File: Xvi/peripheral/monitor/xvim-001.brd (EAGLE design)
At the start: 47 x 72 mm, 7 parts

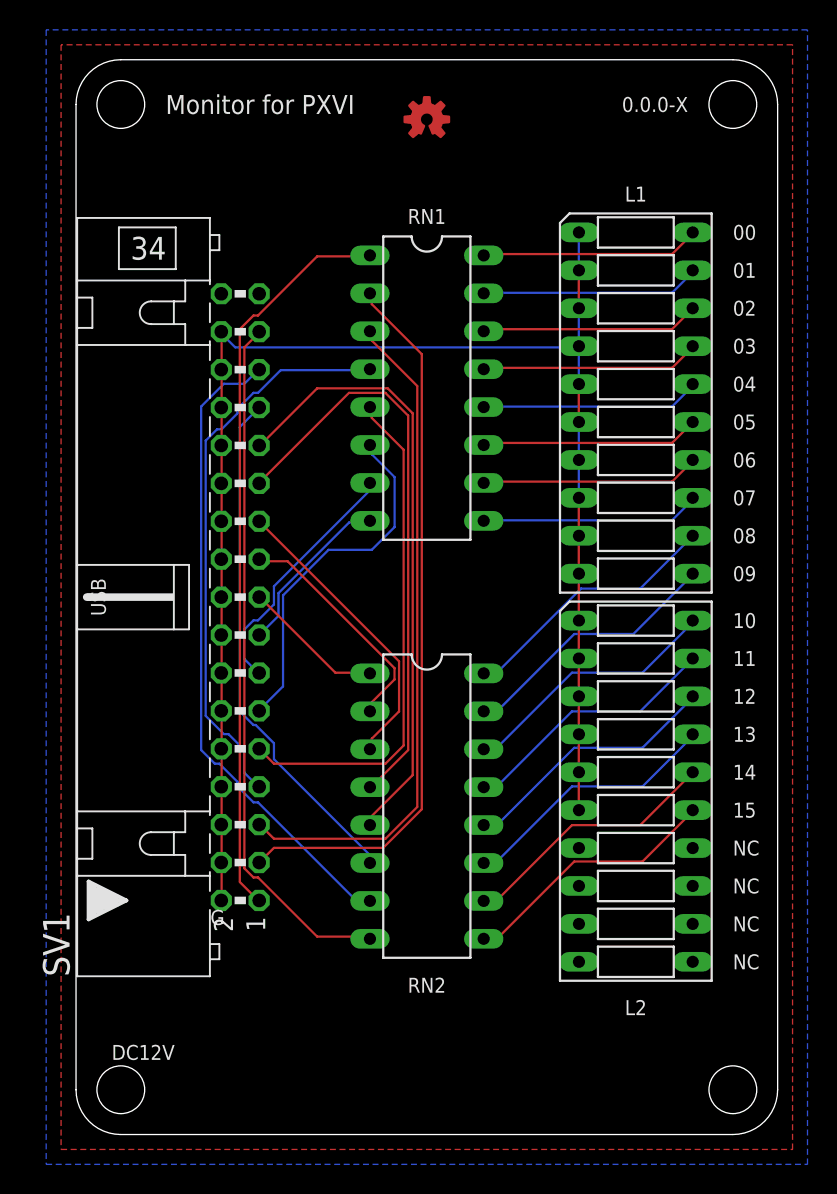
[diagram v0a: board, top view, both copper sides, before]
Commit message: Fixed positioning error of Monitor for PXVI.
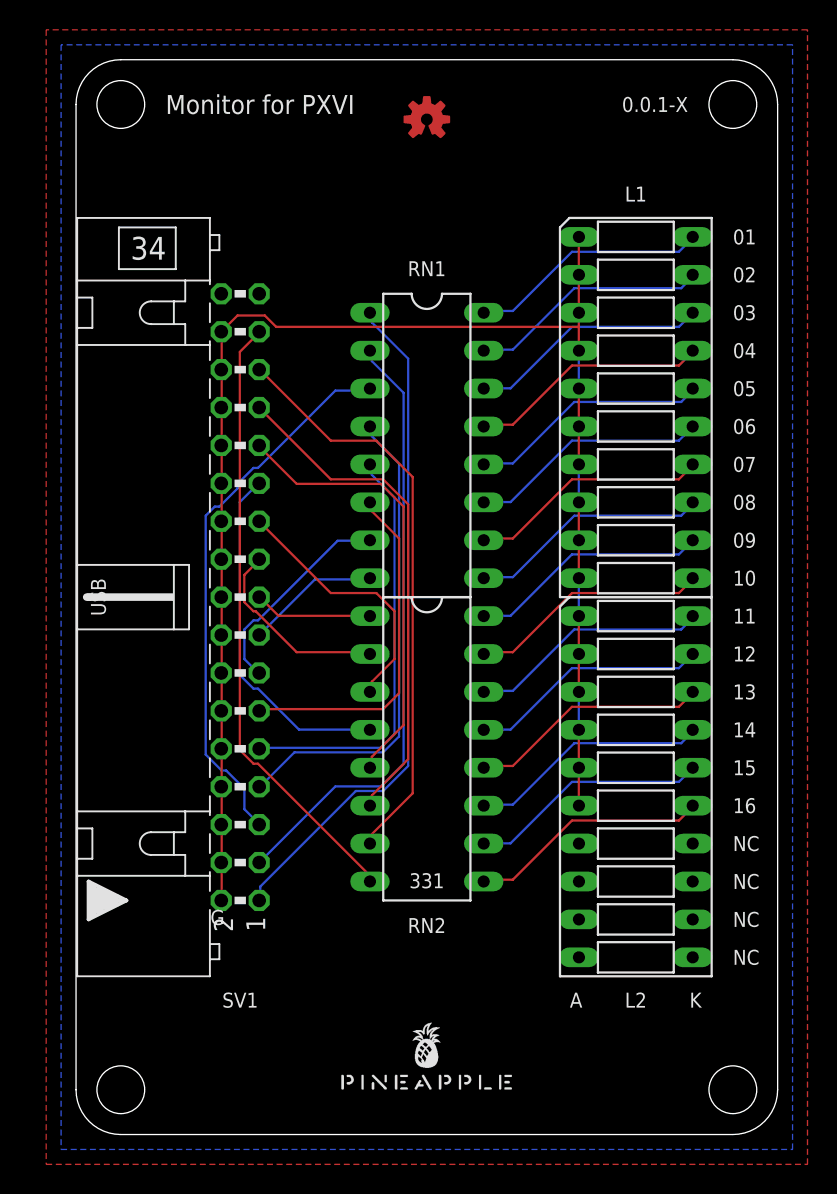
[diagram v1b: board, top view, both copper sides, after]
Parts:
- moved U$1 30.5 mm to (23.5, 3.00), flipped to the top
- moved RN1 3.84 mm to (23.5, 46.2)
- moved RN2 3.84 mm to (23.5, 25.8)
- moved L2 0.30 mm to (37.5, 23.3)
- moved L1 0.30 mm to (37.5, 48.7)
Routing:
- net LD11: track 39.1 -> 23.6 mm
- net LD12: track 41.3 -> 29.8 mm
- net LD02: track 45.1 -> 37.1 mm
- net LD01: track 48.4 -> 41.0 mm
- net LD04: track 34.2 -> 28.2 mm
- net LD03: track 38.1 -> 32.4 mm
- net LD15: track 46.8 -> 41.1 mm
- net LD14: track 43.6 -> 39.1 mm
- net LD00: track 49.6 -> 45.7 mm
- net LD06: track 16.8 -> 14.2 mm
- net LD09: track 15.7 -> 13.2 mm
- net LD07: track 11.5 -> 9.02 mm
- net LD10: track 20.0 -> 17.7 mm
- net N$4: track 17.9 -> 16.1 mm
- net N$3: track 17.8 -> 16.1 mm
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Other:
- board text added: "0.0.1-X"
- board text added: "16"
- board text added: "331"
- board text added: "A"
- board text added: "K"
- board text removed: "0.0.0-X"
- board text removed: "00"
- board text removed: "DC12V"

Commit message: Fixed monitor board.
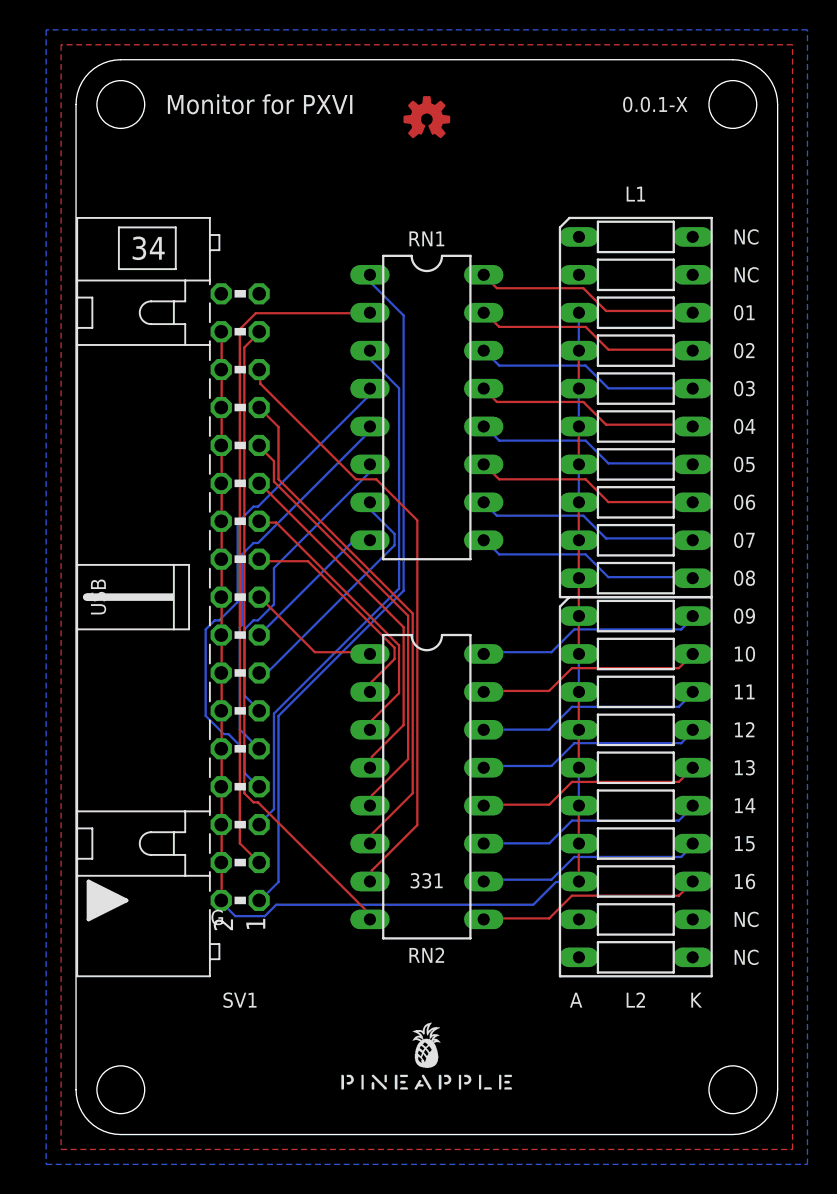
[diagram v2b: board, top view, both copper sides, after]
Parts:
- moved RN1 2.54 mm to (23.5, 48.7)
- moved RN2 2.54 mm to (23.5, 23.3)
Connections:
- removed net LED1K: L1.20, RN1.16
- removed net LED2K: L1.19, RN1.15
- removed net LED3K: L1.18, RN1.14
- removed net LED4K: L1.17, RN1.13
- removed net LED5K: L1.16, RN1.12
- removed net LED6K: L1.15, RN1.11
- new net N$11: L1.12, RN1.10
- new net N$12: L1.14, RN1.12
- new net N$13: L1.15, RN1.13
- new net N$14: L1.16, RN1.14
- new net N$15: L1.17, RN1.15
- new net N$16: L1.18, RN1.16
- net N$1: now also L2.13, RN2.9; no longer L1.14, RN1.10
- net N$10: now also L1.13, RN1.11; no longer L2.15, RN2.9
- net N$2: now also L2.14, RN2.10; no longer L1.13, RN1.9
- net N$3: now also L2.15, RN2.11; no longer L1.12, RN2.16
- net N$4: now also L2.16, RN2.12; no longer L1.11, RN2.15
- net N$5: now also L2.17, RN2.13; no longer L2.20, RN2.14
- net N$6: now also L2.18, RN2.14; no longer L2.19, RN2.13
- net N$7: now also L2.19, RN2.15; no longer L2.18, RN2.12
- net N$8: now also L2.20, RN2.16; no longer L2.17, RN2.11
- net N$9: now also L1.11, RN1.9; no longer L2.16, RN2.10
- net VIN: now also L2.7, L2.8; no longer L1.1, L1.2
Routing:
- net LED2K: track 16.2 -> 0.00 mm
- net LED5K: track 16.2 -> 0.00 mm
- net LED1K: track 16.1 -> 0.00 mm
- net LED4K: track 16.1 -> 0.00 mm
- net LED6K: track 16.1 -> 0.00 mm
- net LED3K: track 16.1 -> 0.00 mm
- net N$16: track 0.00 -> 15.1 mm
- net N$13: track 0.00 -> 15.1 mm
- net N$11: track 0.00 -> 15.1 mm
- net N$15: track 0.00 -> 15.1 mm
- net N$12: track 0.00 -> 15.1 mm
- net N$14: track 0.00 -> 15.0 mm
- net LD01: track 41.0 -> 45.4 mm
- net LD05: track 23.5 -> 20.6 mm
- net LD04: track 28.2 -> 25.9 mm
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
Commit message: Fixed positions of the components.
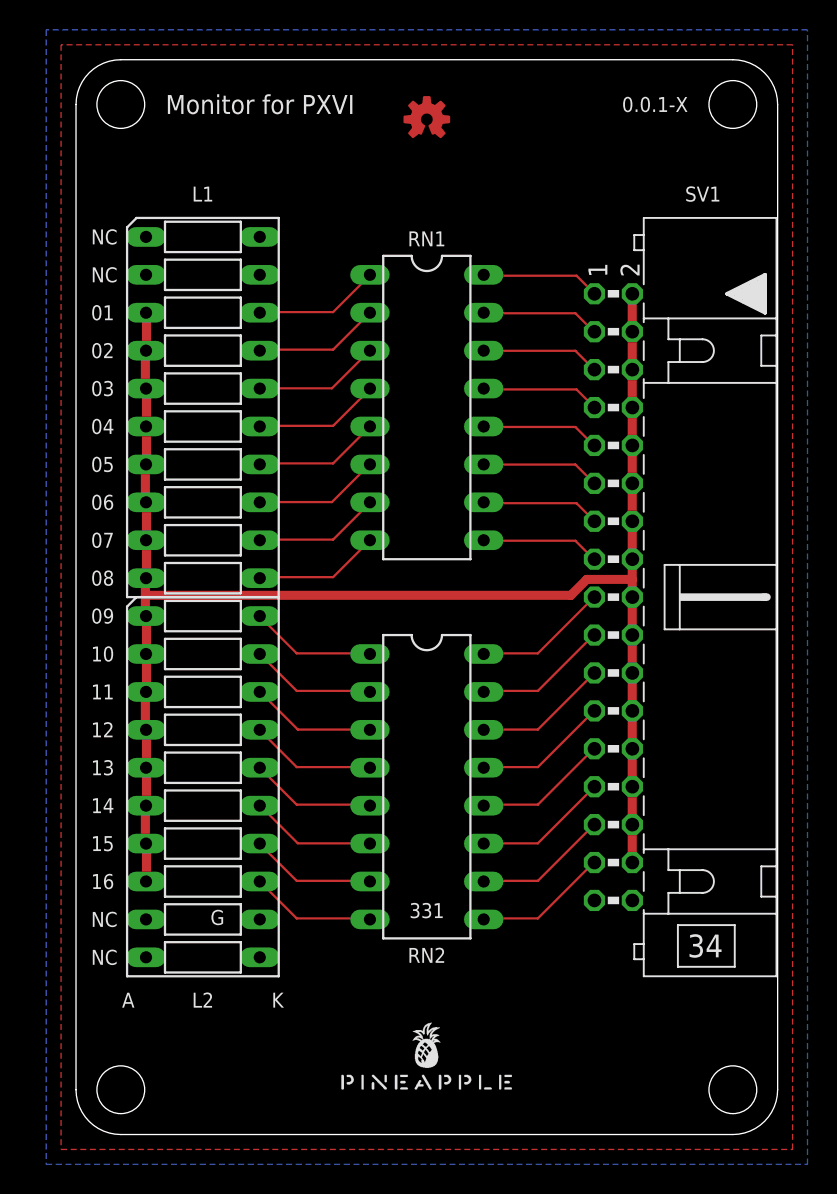
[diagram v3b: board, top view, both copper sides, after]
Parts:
- RN2: value 100 -> 330
- moved L1 29.0 mm to (8.50, 48.7)
- moved L2 29.0 mm to (8.50, 23.3)
- moved SV1 25.0 mm to (36.0, 36.0), turned to 270 degrees
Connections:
- new net GND: SV1.34
- new net MNTR: SV1.33
- net LD00: now also RN1.16; no longer RN1.1
- net LD01: now also RN1.15; no longer RN1.2
- net LD02: now also RN1.14; no longer RN1.3
- net LD03: now also RN1.13; no longer RN1.4
- net LD04: now also RN1.12; no longer RN1.5
- net LD05: now also RN1.11; no longer RN1.6
- net LD06: now also RN1.10; no longer RN1.7
- net LD07: now also RN1.9; no longer RN1.8
- net LD08: now also RN2.16; no longer RN2.1
- net LD09: now also RN2.15; no longer RN2.2
- net LD10: now also RN2.14; no longer RN2.3
- net LD11: now also RN2.13; no longer RN2.4
- net LD12: now also RN2.12; no longer RN2.5
- net LD13: now also RN2.11; no longer RN2.6
- net LD14: now also RN2.10; no longer RN2.7
- net LD15: now also RN2.9; no longer RN2.8
- net N$1: now also L1.18, RN1.1; no longer L2.13, RN2.9
- net N$10: now also L2.19, RN2.2; no longer L1.13, RN1.11
- net N$11: now also L2.18, RN2.3; no longer L1.12, RN1.10
- net N$12: now also L2.17, RN2.4; no longer L1.14, RN1.12
- net N$13: now also L2.16, RN2.5; no longer L1.15, RN1.13
- net N$14: now also L2.15, RN2.6; no longer L1.16, RN1.14
- net N$15: now also L2.14, RN2.7; no longer L1.17, RN1.15
- net N$16: now also L2.13, RN2.8; no longer L1.18, RN1.16
- net N$2: now also L1.17, RN1.2; no longer L2.14, RN2.10
- net N$3: now also L1.16, RN1.3; no longer L2.15, RN2.11
- net N$4: now also L1.15, RN1.4; no longer L2.16, RN2.12
- net N$5: now also L1.14, RN1.5; no longer L2.17, RN2.13
- net N$6: now also L1.13, RN1.6; no longer L2.18, RN2.14
- net N$7: now also L1.12, RN1.7; no longer L2.19, RN2.15
- net N$8: now also L1.11, RN1.8; no longer L2.20, RN2.16
- net N$9: now also L2.20, RN2.1; no longer L1.11, RN1.9
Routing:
- net LD00: track 46.9 -> 7.95 mm
- net LD01: track 45.4 -> 7.94 mm
- net LD15: track 43.4 -> 9.00 mm
- net LD14: track 40.8 -> 8.99 mm
- net LD02: track 36.4 -> 7.94 mm
- net LD13: track 34.7 -> 8.99 mm
- net LD03: track 33.3 -> 7.95 mm
- net LD12: track 29.3 -> 9.00 mm
- net LD04: track 25.9 -> 7.94 mm
- net LD11: track 24.0 -> 8.99 mm
- net LD05: track 20.6 -> 7.94 mm
- net LD10: track 19.3 -> 8.99 mm
- net LD06: track 16.2 -> 7.95 mm
- net VIN: track 101.8 -> 109.6 mm
- net N$11: track 15.1 -> 8.43 mm
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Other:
- board text removed: "USB"
